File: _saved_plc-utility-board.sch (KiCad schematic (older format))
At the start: 11 parts, among them J1 Screw_Terminal_01x02, J10 Screw_Terminal_01x03, J11 Screw_Terminal_01x02, J2 Screw_Terminal_01x08, J3 Screw_Terminal_01x04, J4 Screw_Terminal_01x08, J5 TerminalBlock_02x04, J6 Conn_01x03_Male, J7 Conn_01x03_Male, J8 Screw_Terminal_01x03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

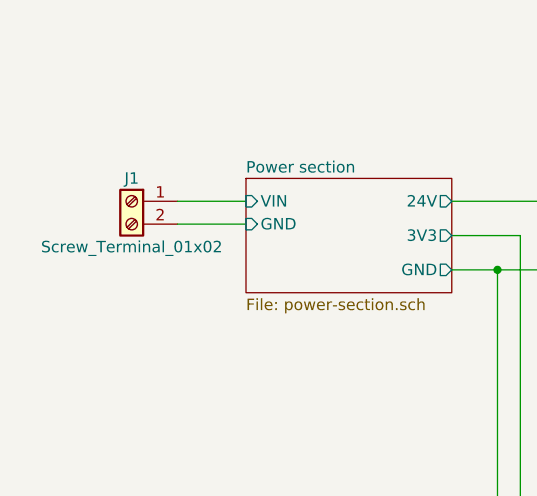
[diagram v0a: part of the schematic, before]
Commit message: Added power supply section to PCB. Added missing components footprints.
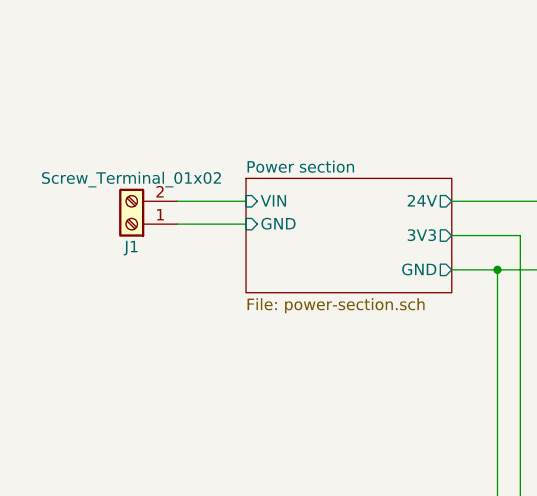
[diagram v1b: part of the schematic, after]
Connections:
- net Power section/GND: now also J1.1 (Pin_1); no longer J1.2 (Pin_2)
- net Power section/VIN: now also J1.2 (Pin_2); no longer J1.1 (Pin_1)
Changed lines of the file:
@@
 L Connector:Screw_Terminal_01x02 J1
 U 1 1 5BF6D1F4
-P 1250 1500
-F 0 "J1" H 1250 1600 50  0000 C CNN
-F 1 "Screw_Terminal_01x02" H 1250 1300 50  0000 C CNN
-F 2 "TerminalBlock:TerminalBlock_bornier-2_P5.08mm" H 1250 1500 50  0001 C CNN
-F 3 "~" H 1250 1500 50  0001 C CNN
-	1    1250 1500
-	-1   0    0    -1
+P 1250 1600
+F 0 "J1" H 1250 1700 50  0000 C CNN
+F 1 "Screw_Terminal_01x02" H 1250 1400 50  0000 C CNN
+F 2 "TerminalBlock:TerminalBlock_bornier-2_P5.08mm" H 1250 1600 50  0001 C CNN
+F 3 "~" H 1250 1600 50  0001 C CNN
+	1    1250 1600
+	-1   0    0    1
 $EndComp
 Wire Wire Line
